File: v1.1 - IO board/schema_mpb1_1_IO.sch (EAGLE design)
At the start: 82 parts

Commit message: First Revision
- Added 3 PIN terminal block for power
- Cleaned up tracks /rerouted
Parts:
- removed JP1: (no value), pinhead:PINHD-2X10
- added I/O1: (no value), pinhead-2:PINHD-2X10_2.54
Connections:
- new net +12V: I/O1.20
- new net +5V: I/O1.19
- new net 3.3V: I/O1.17
- new net VIN: I/O1.18
- net GND: now also I/O1.15, I/O1.16
- net PE0: now also I/O1.1
- net PE1: now also I/O1.2
- net PE10: now also I/O1.11
- net PE11: now also I/O1.12
- net PE12: now also I/O1.13
- net PE13: now also I/O1.14
- net PE2: now also I/O1.3
- net PE3: now also I/O1.4
- net PE4: now also I/O1.5
- net PE5: now also I/O1.6
- net PE6: now also I/O1.7
- net PE7: now also I/O1.8
- net PE8: now also I/O1.9
- net PE9: now also I/O1.10

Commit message: IO board tracks
- Routed first version of IO board, added dimensions
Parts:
- added JP1: (no value), pinhead:PINHD-1X3
- added P1, P2, P3, P4, P5, P6, P7: (no value), jumper:SJ2WW
- DIR10, DIR11, DIR12, DIR13, DIR14, DIR8, DIR9: device jumper:SJ2WW -> jumper:SJ2W
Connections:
- removed net 3.3V: I/O1.17
- new net COM4: 0C11.EMIT, X3-7.KL
- new net P1: P1.2, X1-1.KL
- new net P2: P2.2, X1-4.KL
- new net P3: P3.2, X1-7.KL
- new net P4: P4.2, X1-10.KL
- new net P5: P5.2, X2-2.KL
- new net P6: P6.2, X2-5.KL
- new net P7: P7.2, X2-8.KL
- net +12V: now also I/O1.19, P1.3, P2.3, P3.3, P4.3, P5.3, P6.3, P7.3; no longer I/O1.20
- net +3V3: now also I/O1.18, JP1.1
- net +5V: now also I/O1.20, JP1.2; no longer I/O1.19
- net COM1: now also X3-1.KL
- net COM2: now also X3-3.KL
- net COM3: now also X3-5.KL
- net COM5: now also X3-9.KL; no longer 0C11.EMIT
- net COM6: now also X3-11.KL
- net COM7: now also X4-2.KL
- net GND: now also JP1.3, X1-3.KL, X1-6.KL, X1-9.KL, X2-1.KL, X2-10.KL, X2-4.KL, X2-7.KL
- net IO1: now also X1-2.KL
- net IO2: now also X1-5.KL
- net IO3: now also X1-8.KL
- net IO4: now also X1-11.KL
- net IO5: now also X2-3.KL
- net IO6: now also X2-6.KL
- net IO7: now also X2-9.KL
- net OUT1: now also X2-11.KL
- net OUT2: now also X3-2.KL
- net OUT3: now also X3-4.KL
- net OUT4: now also X3-6.KL
- net OUT5: now also X3-8.KL
- net OUT6: now also X3-10.KL
- net OUT7: now also X4-1.KL
- net PE0: now also DIR8.1, I/O1.2; no longer DIR1.1, I/O1.1, IO1.1, R2.2
- net PE1: now also DIR9.1, I/O1.1; no longer DIR2.1, I/O1.2, IO2.1, R4.2
- net PE10: now also DIR4.1, I/O1.12, IO4.1, R8.2; no longer DIR11.1, I/O1.11
- net PE11: now also DIR5.1, I/O1.11, IO5.1, R10.2; no longer DIR12.1, I/O1.12
- net PE12: now also DIR6.1, I/O1.14, IO6.1, R12.2; no longer DIR13.1, I/O1.13
- net PE13: now also DIR7.1, I/O1.13, IO7.1, R14.2; no longer DIR14.1, I/O1.14
- net PE2: now also DIR10.1, I/O1.4; no longer DIR3.1, I/O1.3, IO3.1, R6.2
- net PE3: now also DIR11.1, I/O1.3; no longer DIR4.1, I/O1.4, IO4.1, R8.2
- net PE4: now also DIR12.1, I/O1.6; no longer DIR5.1, I/O1.5, IO5.1, R10.2
- net PE5: now also DIR13.1, I/O1.5; no longer DIR6.1, I/O1.6, IO6.1, R12.2
- net PE6: now also DIR14.1, I/O1.8; no longer DIR7.1, I/O1.7, IO7.1, R14.2
- net PE7: now also DIR1.1, I/O1.7, IO1.1, R2.2; no longer DIR8.1, I/O1.8
- net PE8: now also DIR2.1, I/O1.10, IO2.1, R4.2; no longer DIR9.1, I/O1.9
- net PE9: now also DIR3.1, I/O1.9, IO3.1, R6.2; no longer DIR10.1, I/O1.10
- net VIN: now also I/O1.17, P1.1, P2.1, P3.1, P4.1, P5.1, P6.1, P7.1; no longer I/O1.18
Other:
- moved on the sheet: X1-1, X1-10, X1-11, X1-2, X1-3, X1-4, X1-5, X1-6, X1-7, X1-8, X1-9, X2-1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

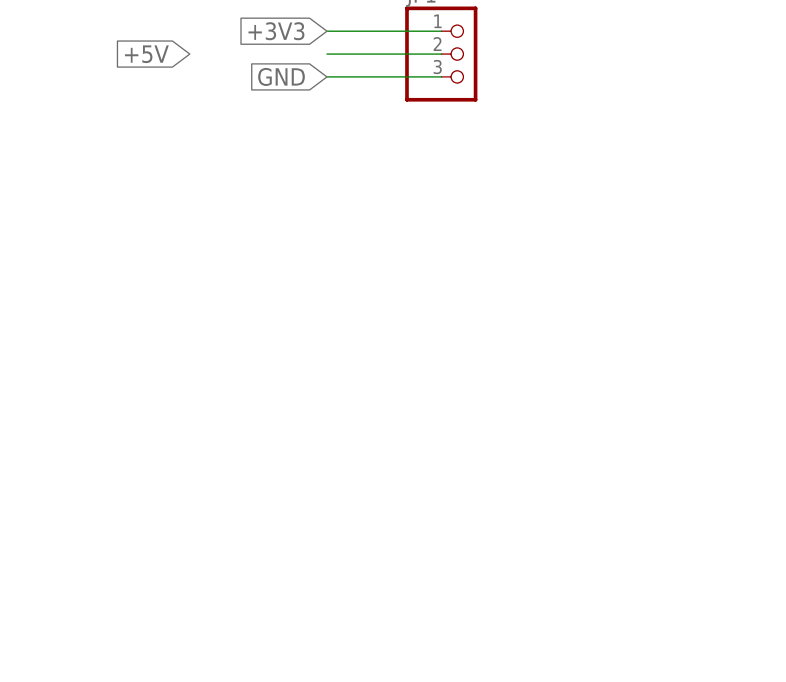
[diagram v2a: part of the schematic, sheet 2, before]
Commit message: IO Board revision
- Fixed GND airwires
- Resolved width errors
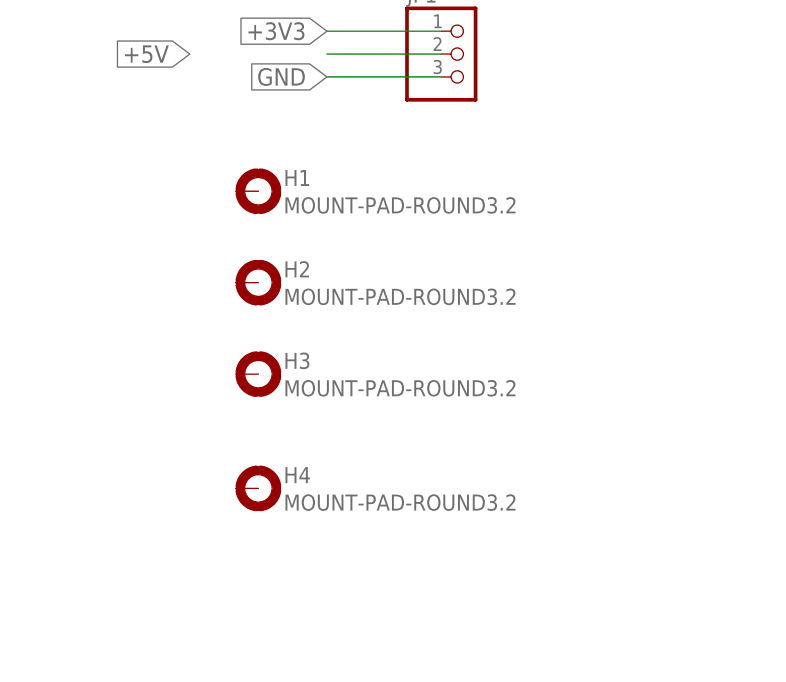
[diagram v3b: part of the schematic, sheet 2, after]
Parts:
- added H1, H2, H3, H4: MOUNT-PAD-ROUND3.2, holes:MOUNT-PAD-ROUND3.2
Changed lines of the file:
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@@
 <part name="P7" library="jumper" library_urn="urn:adsk.eagle:library:252" deviceset="SJ2W" device="W" package3d_urn="urn:adsk.eagle:package:15476/1"/>
 <part name="JP1" library="pinhead" library_urn="urn:adsk.eagle:library:325" deviceset="PINHD-1X3" device="" package3d_urn="urn:adsk.eagle:package:22458/2"/>
+<part name="H1" library="holes" library_urn="urn:adsk.eagle:library:237" deviceset="MOUNT-PAD-ROUND" device="3.2" package3d_urn="urn:adsk.eagle:package:14282/1"/>
+<part name="H2" library="holes" library_urn="urn:adsk.eagle:library:237" deviceset="MOUNT-PAD-ROUND" device="3.2" package3d_urn="urn:adsk.eagle:package:14282/1"/>
+<part name="H3" library="holes" library_urn="urn:adsk.eagle:library:237" deviceset="MOUNT-PAD-ROUND" device="3.2" package3d_urn="urn:adsk.eagle:package:14282/1"/>
+<part name="H4" library="holes" library_urn="urn:adsk.eagle:library:237" deviceset="MOUNT-PAD-ROUND" device="3.2" package3d_urn="urn:adsk.eagle:package:14282/1"/>
 </parts>
 <sheets>
@@
 <instance part="P7" gate="G$1" x="102.362" y="21.082" rot="MR0"/>
 <instance part="JP1" gate="A" x="261.62" y="172.72"/>
+<instance part="H1" gate="G$1" x="238.76" y="157.48"/>
+<instance part="H2" gate="G$1" x="238.76" y="147.32"/>
+<instance part="H3" gate="G$1" x="238.76" y="137.16"/>
+<instance part="H4" gate="G$1" x="238.76" y="124.46"/>
 </instances>
 <busses>

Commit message: IO board. Routing from connector changed. GND vias added
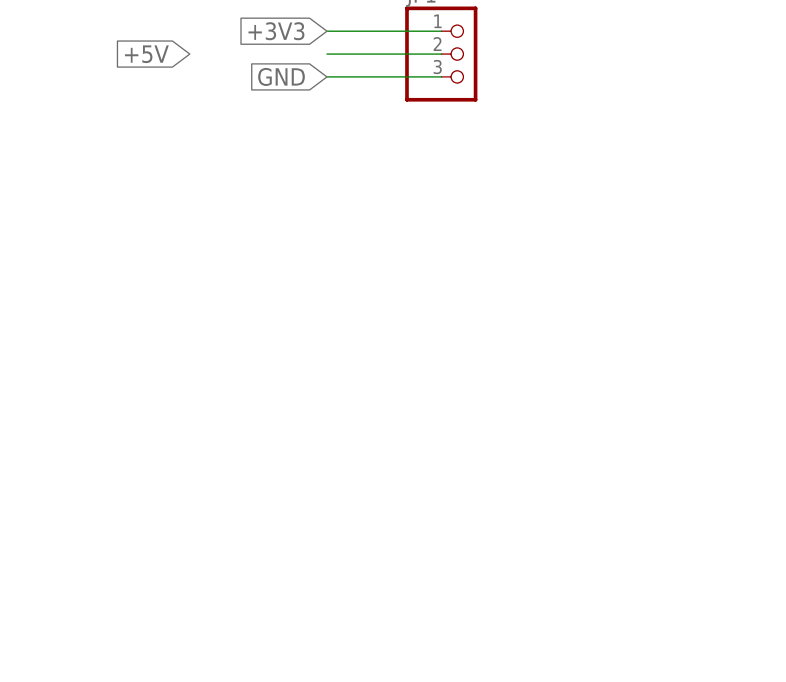
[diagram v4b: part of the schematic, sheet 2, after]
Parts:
- removed H1, H2, H3, H4: MOUNT-PAD-ROUND3.2, holes:MOUNT-PAD-ROUND3.2
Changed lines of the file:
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@@
 <?xml version="1.0" encoding="utf-8"?>
 <!DOCTYPE eagle SYSTEM "eagle.dtd">
-<eagle version="9.0.1">
+<eagle version="9.1.3">
 <drawing>
 <settings>
@@
 <grid distance="0.1" unitdist="inch" unit="mm" style="dots" multiple="1" display="yes" altdistance="0.01" altunitdist="inch" altunit="inch"/>
 <layers>
-<layer number="1" name="Top" color="4" fill="1" visible="yes" active="no"/>
-<layer number="2" name="Route2" color="1" fill="3" visible="yes" active="no"/>
-<layer number="3" name="Route3" color="4" fill="3" visible="yes" active="no"/>
-<layer number="4" name="Route4" color="1" fill="4" visible="yes" active="no"/>
-<layer number="5" name="Route5" color="4" fill="4" visible="yes" active="no"/>
-<layer number="6" name="Route6" color="1" fill="8" visible="yes" active="no"/>
-<layer number="7" name="Route7" color="4" fill="8" visible="yes" active="no"/>
-<layer number="8" name="Route8" color="1" fill="2" visible="yes" active="no"/>
-<layer number="9" name="Route9" color="4" fill="2" visible="yes" active="no"/>
-<layer number="10" name="Route10" color="1" fill="7" visible="yes" active="no"/>
-<layer number="11" name="Route11" color="4" fill="7" visible="yes" active="no"/>
-<layer number="12" name="Route12" color="1" fill="5" visible="yes" active="no"/>
-<layer number="13" name="Route13" color="4" fill="5" visible="yes" active="no"/>
-<layer number="14" name="Route14" color="1" fill="6" visible="yes" active="no"/>
-<layer number="15" name="Route15" color="4" fill="6" visible="yes" active="no"/>
-<layer number="16" name="Bottom" color="1" fill="1" visible="yes" active="no"/>
-<layer number="17" name="Pads" color="2" fill="1" visible="yes" active="no"/>
-<layer number="18" name="Vias" color="2" fill="1" visible="yes" active="no"/>
-<layer number="19" name="Unrouted" color="6" fill="1" visible="yes" active="no"/>
-<layer number="20" name="Dimension" color="24" fill="1" visible="yes" active="no"/>
-<layer number="21" name="tPlace" color="7" fill="1" visible="yes" active="no"/>
-<layer number="22" name="bPlace" color="7" fill="1" visible="yes" active="no"/>
-<layer number="23" name="tOrigins" color="15" fill="1" visible="yes" active="no"/>
-<layer number="24" name="bOrigins" color="15" fill="1" visible="yes" active="no"/>
-<layer number="25" name="tNames" color="7" fill="1" visible="yes" active="no"/>
-<layer number="26" name="bNames" color="7" fill="1" visible="yes" active="no"/>
-<layer number="27" name="tValues" color="7" fill="1" visible="yes" active="no"/>
-<layer number="28" name="bValues" color="7" fill="1" visible="yes" active="no"/>
+<layer number="1" name="Top" color="4" fill="1" visible="no" active="no"/>
+<layer number="2" name="Route2" color="1" fill="3" visible="no" active="no"/>
+<layer number="3" name="Route3" color="4" fill="3" visible="no" active="no"/>
+<layer number="4" name="Route4" color="1" fill="4" visible="no" active="no"/>
+<layer number="5" name="Route5" color="4" fill="4" visible="no" active="no"/>
+<layer number="6" name="Route6" color="1" fill="8" visible="no" active="no"/>
+<layer number="7" name="Route7" color="4" fill="8" visible="no" active="no"/>
+<layer number="8" name="Route8" color="1" fill="2" visible="no" active="no"/>
+<layer number="9" name="Route9" color="4" fill="2" visible="no" active="no"/>
+<layer number="10" name="Route10" color="1" fill="7" visible="no" active="no"/>
+<layer number="11" name="Route11" color="4" fill="7" visible="no" active="no"/>
+<layer number="12" name="Route12" color="1" fill="5" visible="no" active="no"/>
+<layer number="13" name="Route13" color="4" fill="5" visible="no" active="no"/>
+<layer number="14" name="Route14" color="1" fill="6" visible="no" active="no"/>
+<layer number="15" name="Route15" color="4" fill="6" visible="no" active="no"/>
+<layer number="16" name="Bottom" color="1" fill="1" visible="no" active="no"/>
+<layer number="17" name="Pads" color="2" fill="1" visible="no" active="no"/>
+<layer number="18" name="Vias" color="2" fill="1" visible="no" active="no"/>
+<layer number="19" name="Unrouted" color="6" fill="1" visible="no" active="no"/>
+<layer number="20" name="Dimension" color="24" fill="1" visible="no" active="no"/>
+<layer number="21" name="tPlace" color="7" fill="1" visible="no" active="no"/>
+<layer number="22" name="bPlace" color="7" fill="1" visible="no" active="no"/>
+<layer number="23" name="tOrigins" color="15" fill="1" visible="no" active="no"/>
+<layer number="24" name="bOrigins" color="15" fill="1" visible="no" active="no"/>
+<layer number="25" name="tNames" color="7" fill="1" visible="no" active="no"/>
+<layer number="26" name="bNames" color="7" fill="1" visible="no" active="no"/>
+<layer number="27" name="tValues" color="7" fill="1" visible="no" active="no"/>
+<layer number="28" name="bValues" color="7" fill="1" visible="no" active="no"/>
 <layer number="29" name="tStop" color="7" fill="3" visible="no" active="no"/>
 <layer number="30" name="bStop" color="7" fill="6" visible="no" active="no"/>
@@
 <layer number="35" name="tGlue" color="7" fill="4" visible="no" active="no"/>
 <layer number="36" name="bGlue" color="7" fill="5" visible="no" active="no"/>
-<layer number="37" name="tTest" color="7" fill="1" visible="yes" active="no"/>
-<layer number="38" name="bTest" color="7" fill="1" visible="yes" active="no"/>
+<layer number="37" name="tTest" color="7" fill="1" visible="no" active="no"/>
+<layer number="38" name="bTest" color="7" fill="1" visible="no" active="no"/>
 <layer number="39" name="tKeepout" color="4" fill="11" visible="no" active="no"/>
 <layer number="40" name="bKeepout" color="1" fill="11" visible="no" active="no"/>
@@
 <layer number="44" name="Drills" color="7" fill="1" visible="no" active="no"/>
 <layer number="45" name="Holes" color="7" fill="1" visible="no" active="no"/>
-<layer number="46" name="Milling" color="3" fill="1" visible="yes" active="no"/>
-<layer number="47" name="Measures" color="7" fill="1" visible="yes" active="no"/>
-<layer number="48" name="Document" color="7" fill="1" visible="yes" active="no"/>
-<layer number="49" name="Reference" color="7" fill="1" visible="yes" active="no"/>
-<layer number="50" name="dxf" color="7" fill="1" visible="yes" active="no"/>
-<layer number="51" name="tDocu" color="7" fill="1" visible="yes" active="no"/>
-<layer number="52" name="bDocu" color="7" fill="1" visible="yes" active="no"/>
-<layer number="53" name="tGND_GNDA" color="7" fill="9" visible="yes" active="no"/>
-<layer number="54" name="bGND_GNDA" color="1" fill="9" visible="yes" active="no"/>
-<layer number="56" name="wert" color="7" fill="1" visible="yes" active="no"/>
-<layer number="57" name="tCAD" color="7" fill="1" visible="yes" active="no"/>
-<layer number="59" name="tCarbon" color="7" fill="1" visible="yes" active="no"/>
-<layer number="60" name="bCarbon" color="7" fill="1" visible="yes" active="no"/>
+<layer number="46" name="Milling" color="3" fill="1" visible="no" active="no"/>
+<layer number="47" name="Measures" color="7" fill="1" visible="no" active="no"/>
+<layer number="48" name="Document" color="7" fill="1" visible="no" active="no"/>
+<layer number="49" name="Reference" color="7" fill="1" visible="no" active="no"/>
+<layer number="50" name="dxf" color="7" fill="1" visible="no" active="no"/>
+<layer number="51" name="tDocu" color="7" fill="1" visible="no" active="no"/>
+<layer number="52" name="bDocu" color="7" fill="1" visible="no" active="no"/>
+<layer number="53" name="tGND_GNDA" color="7" fill="9" visible="no" active="no"/>
+<layer number="54" name="bGND_GNDA" color="1" fill="9" visible="no" active="no"/>
+<layer number="56" name="wert" color="7" fill="1" visible="no" active="no"/>
+<layer number="57" name="tCAD" color="7" fill="1" visible="no" active="no"/>
+<layer number="59" name="tCarbon" color="7" fill="1" visible="no" active="no"/>
+<layer number="60" name="bCarbon" color="7" fill="1" visible="no" active="no"/>
 <layer number="88" name="SimResults" color="9" fill="1" visible="yes" active="yes"/>
 <layer number="89" name="SimProbes" color="9" fill="1" visible="yes" active="yes"/>
@@
 <part name="P7" library="jumper" library_urn="urn:adsk.eagle:library:252" deviceset="SJ2W" device="W" package3d_urn="urn:adsk.eagle:package:15476/1"/>
 <part name="JP1" library="pinhead" library_urn="urn:adsk.eagle:library:325" deviceset="PINHD-1X3" device="" package3d_urn="urn:adsk.eagle:package:22458/2"/>
-<part name="H1" library="holes" library_urn="urn:adsk.eagle:library:237" deviceset="MOUNT-PAD-ROUND" device="3.2" package3d_urn="urn:adsk.eagle:package:14282/1"/>
-<part name="H2" library="holes" library_urn="urn:adsk.eagle:library:237" deviceset="MOUNT-PAD-ROUND" device="3.2" package3d_urn="urn:adsk.eagle:package:14282/1"/>
-<part name="H3" library="holes" library_urn="urn:adsk.eagle:library:237" deviceset="MOUNT-PAD-ROUND" device="3.2" package3d_urn="urn:adsk.eagle:package:14282/1"/>
-<part name="H4" library="holes" library_urn="urn:adsk.eagle:library:237" deviceset="MOUNT-PAD-ROUND" device="3.2" package3d_urn="urn:adsk.eagle:package:14282/1"/>
 </parts>
 <sheets>
@@
 <instance part="P7" gate="G$1" x="102.362" y="21.082" rot="MR0"/>
 <instance part="JP1" gate="A" x="261.62" y="172.72"/>
-<instance part="H1" gate="G$1" x="238.76" y="157.48"/>
-<instance part="H2" gate="G$1" x="238.76" y="147.32"/>
-<instance part="H3" gate="G$1" x="238.76" y="137.16"/>
-<instance part="H4" gate="G$1" x="238.76" y="124.46"/>
 </instances>
 <busses>

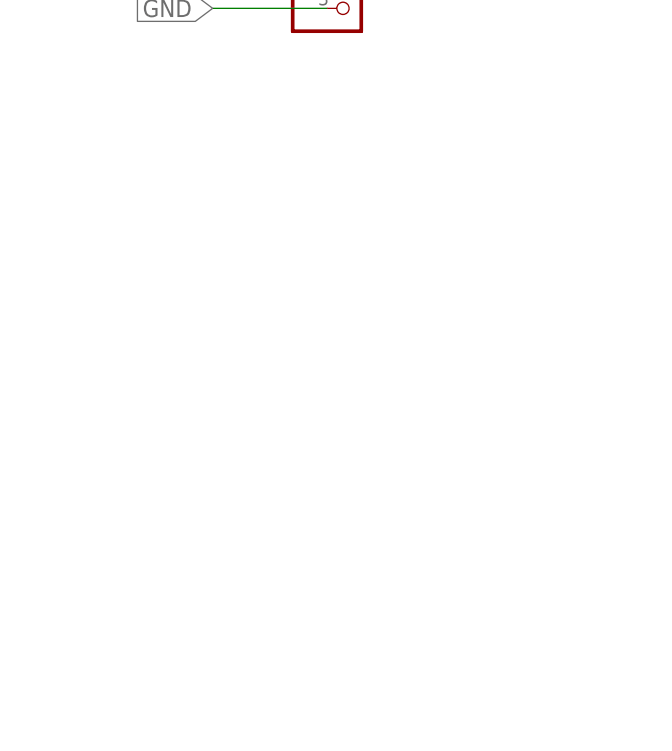
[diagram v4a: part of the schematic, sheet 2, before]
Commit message: IO board
- Added mounting holes and terminal labels
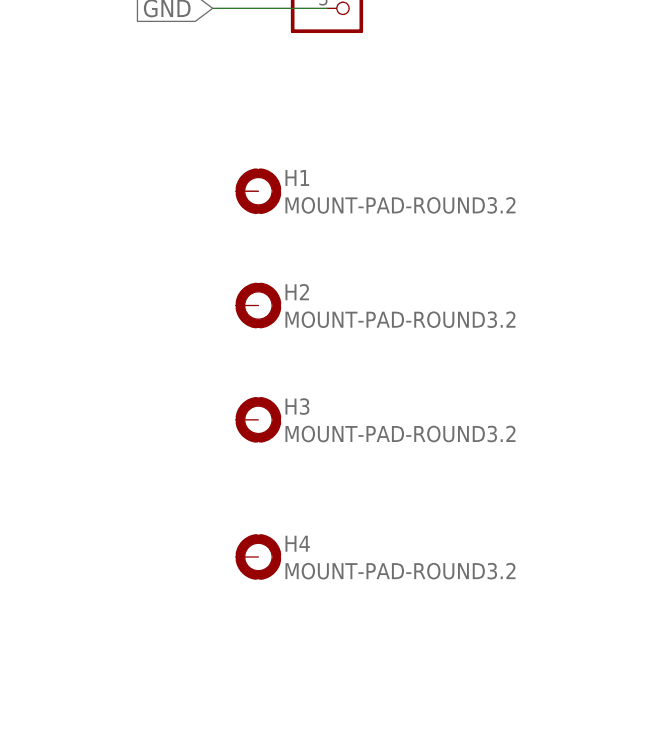
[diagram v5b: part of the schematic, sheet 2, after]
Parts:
- added H1, H2, H3, H4: MOUNT-PAD-ROUND3.2, holes:MOUNT-PAD-ROUND3.2
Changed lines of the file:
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@@
 <?xml version="1.0" encoding="utf-8"?>
 <!DOCTYPE eagle SYSTEM "eagle.dtd">
-<eagle version="9.1.3">
+<eagle version="9.0.1">
 <drawing>
 <settings>
@@
 <part name="P7" library="jumper" library_urn="urn:adsk.eagle:library:252" deviceset="SJ2W" device="W" package3d_urn="urn:adsk.eagle:package:15476/1"/>
 <part name="JP1" library="pinhead" library_urn="urn:adsk.eagle:library:325" deviceset="PINHD-1X3" device="" package3d_urn="urn:adsk.eagle:package:22458/2"/>
+<part name="H1" library="holes" library_urn="urn:adsk.eagle:library:237" deviceset="MOUNT-PAD-ROUND" device="3.2" package3d_urn="urn:adsk.eagle:package:14282/1"/>
+<part name="H2" library="holes" library_urn="urn:adsk.eagle:library:237" deviceset="MOUNT-PAD-ROUND" device="3.2" package3d_urn="urn:adsk.eagle:package:14282/1"/>
+<part name="H3" library="holes" library_urn="urn:adsk.eagle:library:237" deviceset="MOUNT-PAD-ROUND" device="3.2" package3d_urn="urn:adsk.eagle:package:14282/1"/>
+<part name="H4" library="holes" library_urn="urn:adsk.eagle:library:237" deviceset="MOUNT-PAD-ROUND" device="3.2" package3d_urn="urn:adsk.eagle:package:14282/1"/>
 </parts>
 <sheets>
@@
 <instance part="P7" gate="G$1" x="102.362" y="21.082" rot="MR0"/>
 <instance part="JP1" gate="A" x="261.62" y="172.72"/>
+<instance part="H1" gate="G$1" x="251.46" y="149.86"/>
+<instance part="H2" gate="G$1" x="251.46" y="137.16"/>
+<instance part="H3" gate="G$1" x="251.46" y="124.46"/>
+<instance part="H4" gate="G$1" x="251.46" y="109.22"/>
 </instances>
 <busses>

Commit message: Logos
Added Geviton Logo to designs
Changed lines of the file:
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@@
+</nets>
+</sheet>
+<sheet>
+<plain>
+</plain>
+<instances>
+</instances>
+<busses>
+</busses>
+<nets>
 </nets>
 </sheet>
